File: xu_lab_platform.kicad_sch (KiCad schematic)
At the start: 0 parts

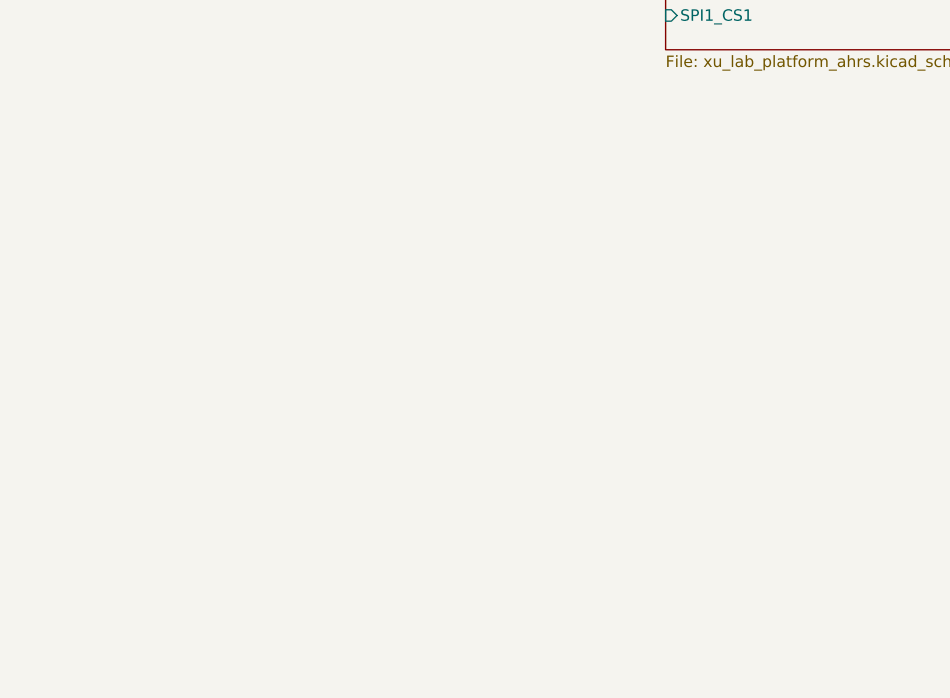
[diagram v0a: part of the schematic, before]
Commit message: Added Pressure Sensor schematic (Bar30 4-pin: 3.3V, GND, SCL, SDA)
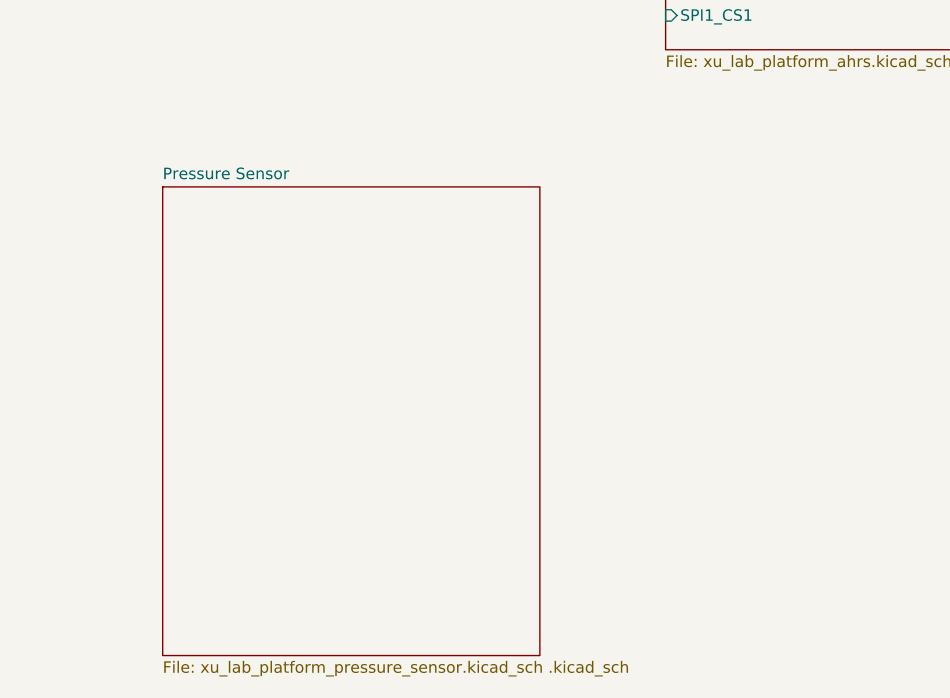
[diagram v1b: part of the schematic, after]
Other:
- added sheet Pressure Sensor (xu_lab_platform_pressure_sensor.kicad_sch .kicad_sch)
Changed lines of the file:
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@@
+	)
+	(sheet
+		(at 114.3 99.06)
+		(size 41.91 52.07)
+		(exclude_from_sim no)
+		(in_bom yes)
+		(on_board yes)
+		(dnp no)
+		(fields_autoplaced yes)
+		(stroke
+			(width 0.1524)
+			(type solid)
+		)
+		(fill
+			(color 0 0 0 0.0000)
+		)
+		(property "Sheetname" "Pressure Sensor"
+			(at 114.3 98.3484 0)
+			(effects
+				(font
+					(size 1.27 1.27)
+				)
+				(justify left bottom)
+			)
+		)
+		(property "Sheetfile" "xu_lab_platform_pressure_sensor.kicad_sch .kicad_sch"
+			(at 114.3 151.7146 0)
+			(effects
+				(font
+					(size 1.27 1.27)
+				)
+				(justify left top)
+			)
+		)
+		(instances
+			(project "xu_lab_platform"
+				(path "/71bb14ae-b730-4d22-a41d-cf68989dae2d"
+					(page "4")
+				)
+			)
+		)
 	)
 	(sheet
